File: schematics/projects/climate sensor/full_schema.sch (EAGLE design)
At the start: 46 parts, among them J1 WAY AMP 4PIN, J10 J2, J11 J2, J12 J4_FS_2, J2 WAY AMP 4PIN, J3 KF301-5.0, J4 KF301-5.0, J5 KF301-5.0, J6 KF301-5.0, J7 KF301-5.0, J8 J2, J9 J2, Q1 2N3904, Q2 2N3904, Q3 2N3904, Q4 2N3904, Q5 2N3904, Q6 2N3904, U1 GY-SGP30, U2 ESP32 DEVKIT WROOM-32D, U3 PMS7003, U4 BH1750, U5 BME280, U6 MH_Z19B

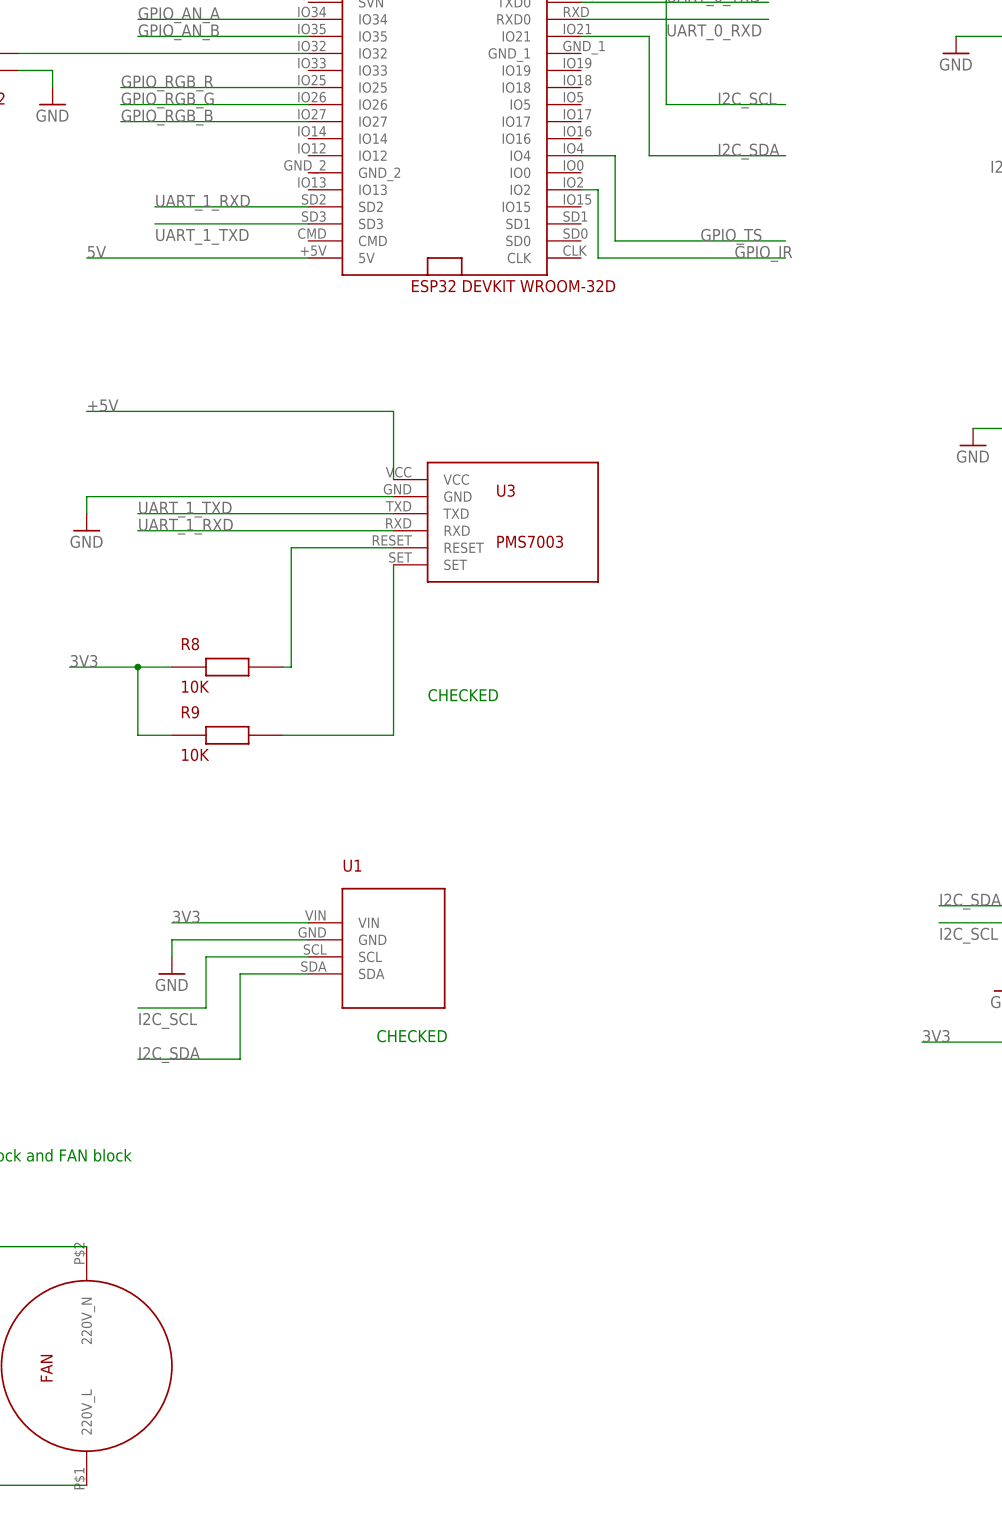
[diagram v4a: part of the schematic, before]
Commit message: FAN PWM speed control - updated driver and schematics. Driver tested on RQD2510LS fan and its worked on 30...100% speed
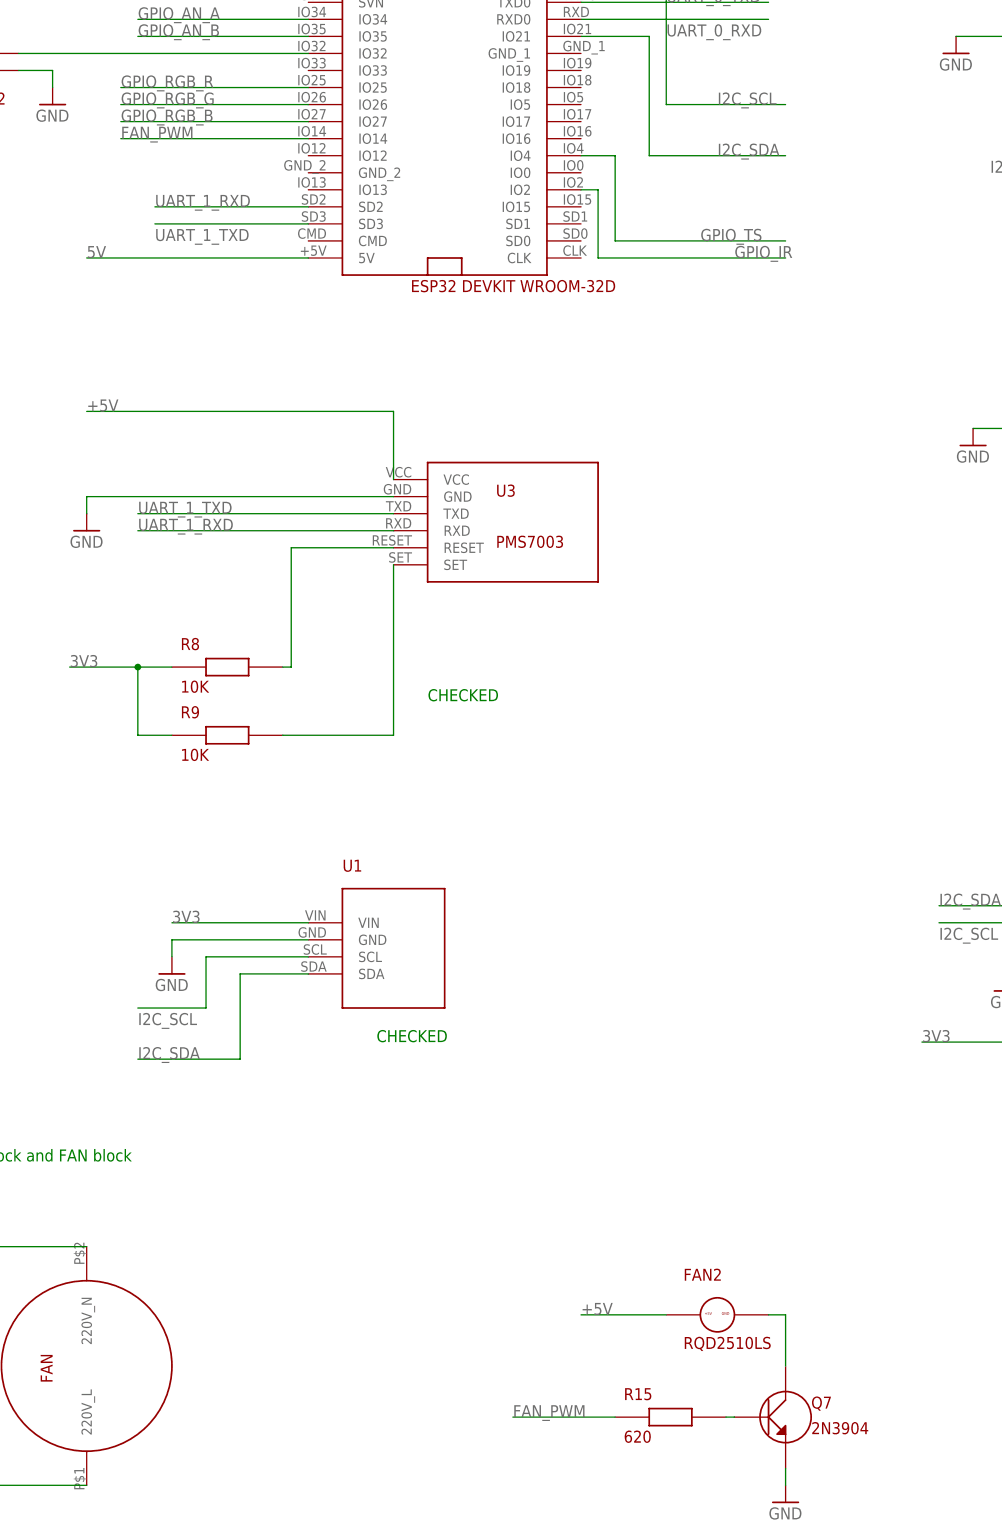
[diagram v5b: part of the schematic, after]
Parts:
- added FAN2: RQD2510LS, my_devices:FAN_5V
- added Q7: 2N3904, my_devices:TRANSISTOR_NPN
- added R15: 620, my_devices:R
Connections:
- new net FAN_PWM: R15.P$1, U2.IO14
- new net N$29: FAN2.GND, Q7.C
- new net N$30: Q7.B, R15.P$2
- net +5V: now also FAN2.VCC
- net GND: now also Q7.E
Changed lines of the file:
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@@
 <schematic_group name="IR"/>
 <schematic_group name="TOUCH_SENSOR"/>
+<schematic_group name="FAN_PWN"/>
 </groups>
 <parts>
@@
 <part name="Q6" library="my_devices" deviceset="TRANSISTOR_NPN" device="" value="2N3904"/>
 <part name="GND7" library="supply1" library_urn="urn:adsk.eagle:library:371" deviceset="GND" device=""/>
+<part name="Q7" library="my_devices" deviceset="TRANSISTOR_NPN" device="" value="2N3904"/>
+<part name="FAN2" library="my_devices" deviceset="FAN_5V" device="" value="RQD2510LS"/>
+<part name="GND8" library="supply1" library_urn="urn:adsk.eagle:library:371" deviceset="GND" device=""/>
+<part name="R15" library="my_devices" deviceset="R" device="" value="620"/>
 </parts>
 <sheets>
@@
 <attribute name="VALUE" x="210.82" y="-10.16" size="1.778" layer="96"/>
 </instance>
+<instance part="Q7" gate="G$1" x="15.24" y="-114.3" smashed="yes" grouprefs="FAN_PWN">
+<attribute name="NAME" x="19.05" y="-113.03" size="1.778" layer="94"/>
+<attribute name="VALUE" x="19.05" y="-116.84" size="1.778" layer="94"/>
+</instance>
+<instance part="FAN2" gate="G$1" x="5.08" y="-99.06" smashed="yes" grouprefs="FAN_PWN">
+<attribute name="NAME" x="0" y="-93.98" size="1.778" layer="94"/>
+<attribute name="VALUE" x="0" y="-104.14" size="1.778" layer="94"/>
+</instance>
+<instance part="GND8" gate="1" x="15.24" y="-127" smashed="yes" grouprefs="FAN_PWN">
+<attribute name="VALUE" x="12.7" y="-129.54" size="1.778" layer="96"/>
+</instance>
+<instance part="R15" gate="G$1" x="-2.54" y="-114.3" smashed="yes" grouprefs="FAN_PWN">
+<attribute name="NAME" x="-8.89" y="-111.76" size="1.778" layer="94"/>
+<attribute name="VALUE" x="-8.89" y="-118.11" size="1.778" layer="94"/>
+</instance>
 </instances>
 <busses>
@@
 <wire x1="213.36" y1="0" x2="213.36" y2="-5.08" width="0.1524" layer="91" grouprefs="RGBLED"/>
 <pinref part="GND7" gate="1" pin="GND"/>
+</segment>
+<segment>
+<pinref part="Q7" gate="G$1" pin="E"/>
+<pinref part="GND8" gate="1" pin="GND"/>
+<wire x1="15.24" y1="-121.92" x2="15.24" y2="-124.46" width="0.1524" layer="91" grouprefs="FAN_PWN"/>
 </segment>
 </net>
@@
 <label x="-88.9" y="35.56" size="1.778" layer="95" grouprefs="PMS7003"/>
 </segment>
+<segment>
+<pinref part="FAN2" gate="G$1" pin="VCC"/>
+<wire x1="-2.54" y1="-99.06" x2="-15.24" y2="-99.06" width="0.1524" layer="91" grouprefs="FAN_PWN"/>
+<label x="-15.24" y="-99.06" size="1.778" layer="95" grouprefs="FAN_PWN"/>
+</segment>
 </net>
 <net name="3V3" class="0">
@@
 </segment>
 </net>
+<net name="N$29" class="0">
+<segment>
+<pinref part="FAN2" gate="G$1" pin="GND"/>
+<pinref part="Q7" gate="G$1" pin="C"/>
+<wire x1="12.7" y1="-99.06" x2="15.24" y2="-99.06" width="0.1524" layer="91" grouprefs="FAN_PWN"/>
+<wire x1="15.24" y1="-99.06" x2="15.24" y2="-106.68" width="0.1524" layer="91" grouprefs="FAN_PWN"/>
+</segment>
+</net>
+<net name="N$30" class="0">
+<segment>
+<pinref part="R15" gate="G$1" pin="P$2"/>
+<pinref part="Q7" gate="G$1" pin="B"/>
+<wire x1="6.35" y1="-114.3" x2="7.62" y2="-114.3" width="0.1524" layer="91" grouprefs="FAN_PWN"/>
+</segment>
+</net>
+<net name="FAN_PWM" class="0">
+<segment>
+<pinref part="R15" gate="G$1" pin="P$1"/>
+<wire x1="-10.16" y1="-114.3" x2="-25.4" y2="-114.3" width="0.1524" layer="91" grouprefs="FAN_PWN"/>
+<label x="-25.4" y="-114.3" size="1.778" layer="95" grouprefs="FAN_PWN"/>
+</segment>
+<segment>
+<pinref part="U2" gate="G$1" pin="IO14"/>
+<wire x1="-55.88" y1="76.2" x2="-83.82" y2="76.2" width="0.1524" layer="91" grouprefs="ESP"/>
+<label x="-83.82" y="76.2" size="1.778" layer="95"/>
+</segment>
+</net>

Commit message: fixes in touchpad sensor
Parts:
- R1, R4: value 600 -> 3K
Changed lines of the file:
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@@
 <grid distance="0.1" unitdist="inch" unit="inch" style="lines" multiple="1" display="no" altdistance="0.01" altunitdist="inch" altunit="inch"/>
 <layers>
-<layer number="1" name="Top" color="4" fill="1" visible="no" active="no"/>
-<layer number="2" name="Route2" color="1" fill="3" visible="no" active="no"/>
-<layer number="3" name="Route3" color="4" fill="3" visible="no" active="no"/>
-<layer number="4" name="Route4" color="1" fill="4" visible="no" active="no"/>
-<layer number="5" name="Route5" color="4" fill="4" visible="no" active="no"/>
-<layer number="6" name="Route6" color="1" fill="8" visible="no" active="no"/>
-<layer number="7" name="Route7" color="4" fill="8" visible="no" active="no"/>
-<layer number="8" name="Route8" color="1" fill="2" visible="no" active="no"/>
-<layer number="9" name="Route9" color="4" fill="2" visible="no" active="no"/>
-<layer number="10" name="Route10" color="1" fill="7" visible="no" active="no"/>
-<layer number="11" name="Route11" color="4" fill="7" visible="no" active="no"/>
-<layer number="12" name="Route12" color="1" fill="5" visible="no" active="no"/>
-<layer number="13" name="Route13" color="4" fill="5" visible="no" active="no"/>
-<layer number="14" name="Route14" color="1" fill="6" visible="no" active="no"/>
-<layer number="15" name="Route15" color="4" fill="6" visible="no" active="no"/>
-<layer number="16" name="Bottom" color="1" fill="1" visible="no" active="no"/>
-<layer number="17" name="Pads" color="2" fill="1" visible="no" active="no"/>
-<layer number="18" name="Vias" color="2" fill="1" visible="no" active="no"/>
-<layer number="19" name="Unrouted" color="6" fill="1" visible="no" active="no"/>
-<layer number="20" name="Dimension" color="15" fill="1" visible="no" active="no"/>
-<layer number="21" name="tPlace" color="7" fill="1" visible="no" active="no"/>
-<layer number="22" name="bPlace" color="7" fill="1" visible="no" active="no"/>
-<layer number="23" name="tOrigins" color="15" fill="1" visible="no" active="no"/>
-<layer number="24" name="bOrigins" color="15" fill="1" visible="no" active="no"/>
-<layer number="25" name="tNames" color="7" fill="1" visible="no" active="no"/>
-<layer number="26" name="bNames" color="7" fill="1" visible="no" active="no"/>
-<layer number="27" name="tValues" color="7" fill="1" visible="no" active="no"/>
-<layer number="28" name="bValues" color="7" fill="1" visible="no" active="no"/>
+<layer number="1" name="Top" color="4" fill="1" visible="yes" active="no"/>
+<layer number="2" name="Route2" color="1" fill="3" visible="yes" active="no"/>
+<layer number="3" name="Route3" color="4" fill="3" visible="yes" active="no"/>
+<layer number="4" name="Route4" color="1" fill="4" visible="yes" active="no"/>
+<layer number="5" name="Route5" color="4" fill="4" visible="yes" active="no"/>
+<layer number="6" name="Route6" color="1" fill="8" visible="yes" active="no"/>
+<layer number="7" name="Route7" color="4" fill="8" visible="yes" active="no"/>
+<layer number="8" name="Route8" color="1" fill="2" visible="yes" active="no"/>
+<layer number="9" name="Route9" color="4" fill="2" visible="yes" active="no"/>
+<layer number="10" name="Route10" color="1" fill="7" visible="yes" active="no"/>
+<layer number="11" name="Route11" color="4" fill="7" visible="yes" active="no"/>
+<layer number="12" name="Route12" color="1" fill="5" visible="yes" active="no"/>
+<layer number="13" name="Route13" color="4" fill="5" visible="yes" active="no"/>
+<layer number="14" name="Route14" color="1" fill="6" visible="yes" active="no"/>
+<layer number="15" name="Route15" color="4" fill="6" visible="yes" active="no"/>
+<layer number="16" name="Bottom" color="1" fill="1" visible="yes" active="no"/>
+<layer number="17" name="Pads" color="2" fill="1" visible="yes" active="no"/>
+<layer number="18" name="Vias" color="2" fill="1" visible="yes" active="no"/>
+<layer number="19" name="Unrouted" color="6" fill="1" visible="yes" active="no"/>
+<layer number="20" name="Dimension" color="15" fill="1" visible="yes" active="no"/>
+<layer number="21" name="tPlace" color="7" fill="1" visible="yes" active="no"/>
+<layer number="22" name="bPlace" color="7" fill="1" visible="yes" active="no"/>
+<layer number="23" name="tOrigins" color="15" fill="1" visible="yes" active="no"/>
+<layer number="24" name="bOrigins" color="15" fill="1" visible="yes" active="no"/>
+<layer number="25" name="tNames" color="7" fill="1" visible="yes" active="no"/>
+<layer number="26" name="bNames" color="7" fill="1" visible="yes" active="no"/>
+<layer number="27" name="tValues" color="7" fill="1" visible="yes" active="no"/>
+<layer number="28" name="bValues" color="7" fill="1" visible="yes" active="no"/>
 <layer number="29" name="tStop" color="7" fill="3" visible="no" active="no"/>
 <layer number="30" name="bStop" color="7" fill="6" visible="no" active="no"/>
@@
 <layer number="35" name="tGlue" color="7" fill="4" visible="no" active="no"/>
 <layer number="36" name="bGlue" color="7" fill="5" visible="no" active="no"/>
-<layer number="37" name="tTest" color="7" fill="1" visible="no" active="no"/>
-<layer number="38" name="bTest" color="7" fill="1" visible="no" active="no"/>
+<layer number="37" name="tTest" color="7" fill="1" visible="yes" active="no"/>
+<layer number="38" name="bTest" color="7" fill="1" visible="yes" active="no"/>
 <layer number="39" name="tKeepout" color="4" fill="11" visible="no" active="no"/>
 <layer number="40" name="bKeepout" color="1" fill="11" visible="no" active="no"/>
@@
 <layer number="44" name="Drills" color="7" fill="1" visible="no" active="no"/>
 <layer number="45" name="Holes" color="7" fill="1" visible="no" active="no"/>
-<layer number="46" name="Milling" color="3" fill="1" visible="no" active="no"/>
-<layer number="47" name="Measures" color="7" fill="1" visible="no" active="no"/>
-<layer number="48" name="Document" color="7" fill="1" visible="no" active="no"/>
-<layer number="49" name="Reference" color="7" fill="1" visible="no" active="no"/>
-<layer number="51" name="tDocu" color="14" fill="1" visible="no" active="no"/>
-<layer number="52" name="bDocu" color="7" fill="1" visible="no" active="no"/>
+<layer number="46" name="Milling" color="3" fill="1" visible="yes" active="no"/>
+<layer number="47" name="Measures" color="7" fill="1" visible="yes" active="no"/>
+<layer number="48" name="Document" color="7" fill="1" visible="yes" active="no"/>
+<layer number="49" name="Reference" color="7" fill="1" visible="yes" active="no"/>
+<layer number="51" name="tDocu" color="14" fill="1" visible="yes" active="no"/>
+<layer number="52" name="bDocu" color="7" fill="1" visible="yes" active="no"/>
 <layer number="88" name="SimResults" color="9" fill="1" visible="yes" active="yes"/>
 <layer number="89" name="SimProbes" color="9" fill="1" visible="yes" active="yes"/>
@@
 <part name="R2" library="my_devices" deviceset="R" device="" value="600"/>
 <part name="R5" library="my_devices" deviceset="R" device="" value="600"/>
-<part name="R1" library="my_devices" deviceset="R" device="" value="600"/>
-<part name="R4" library="my_devices" deviceset="R" device="" value="600"/>
+<part name="R1" library="my_devices" deviceset="R" device="" value="3K"/>
+<part name="R4" library="my_devices" deviceset="R" device="" value="3K"/>
 <part name="R7" library="my_devices" deviceset="R" device="" value="5 om, 2W"/>
 <part name="D1" library="my_devices" deviceset="LD" device="" value="IR"/>
